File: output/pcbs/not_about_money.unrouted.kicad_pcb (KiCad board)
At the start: 2 copper layers, 76.5 x 114.5 mm, 53 parts

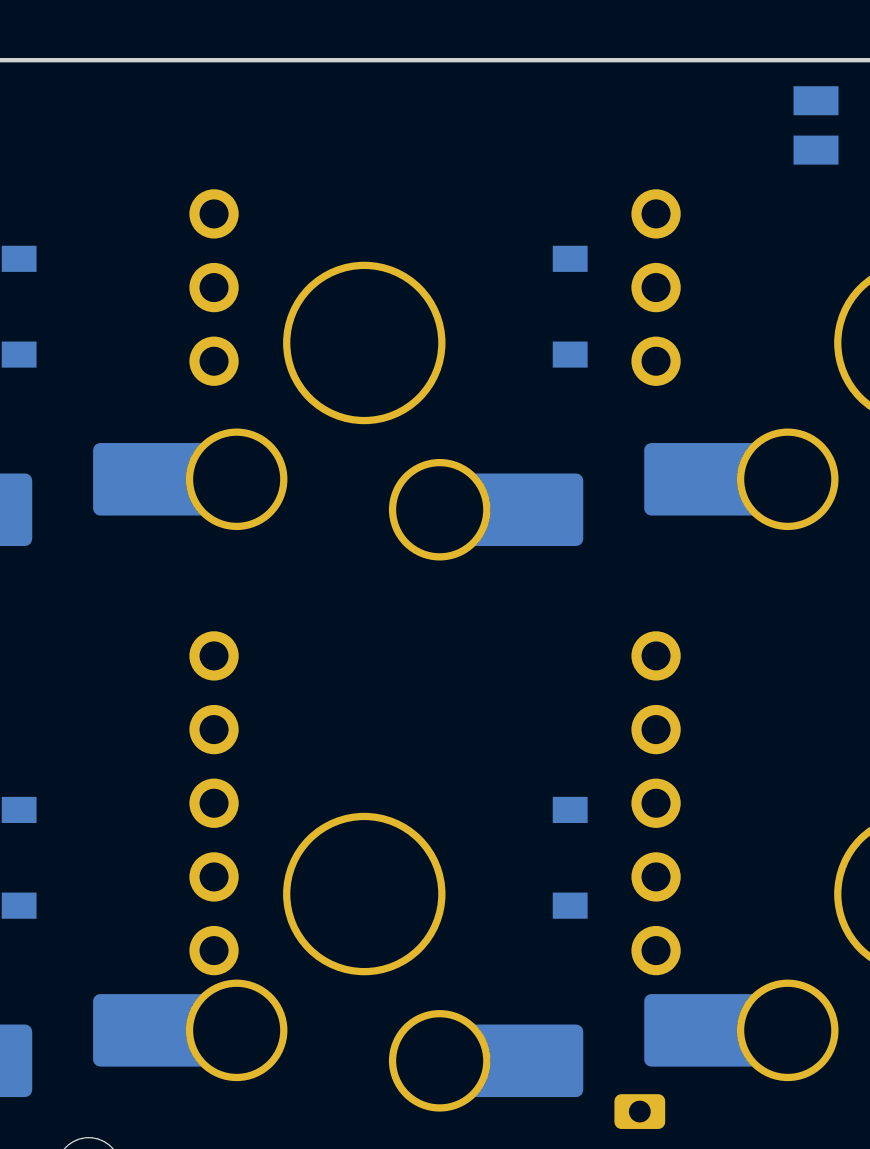
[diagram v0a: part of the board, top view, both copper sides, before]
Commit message: Move nice!nano 1.5mm to the edge, add its CAD model, USB scoop
- nice!nano v2 STEP (kicad/3d/) is now the authority for the case's nano
  and USB-C geometry, and the MCU footprint's 3D model (rotate -90,
  offset 0.11/2.45, verified by exporting the board to STEP).
- MCU moved 1.5mm toward the top edge (KiCad y 13.25 -> 11.75): nano edge
  flush with the PCB edge, USB-C 0.96 past it. Pin clearance improves to
  >=1.51. Re-routed (RAW re-routed alone after freerouting ran it over a
  PWR1 no-net pad); DRC 0 errors, 0 unconnected.
- Case: USB window from the CAD model with 0.25 clearance, a 12.5x6.5 r1.5
  cable-head scoop whose back wall is flush with the USB mouth (collar
  inside the cavity only when the mouth sits behind the wall).
- Fab: kicad/scripts/export_all.sh regenerates fab/, the PCBWay package
  and the board renders; both recipes reproduce the 2026-10-01 exports of
  the old board. All outputs regenerated for the new board.

Co-Authored-By: Claude Opus 5.5 <noreply@anthropic.com>
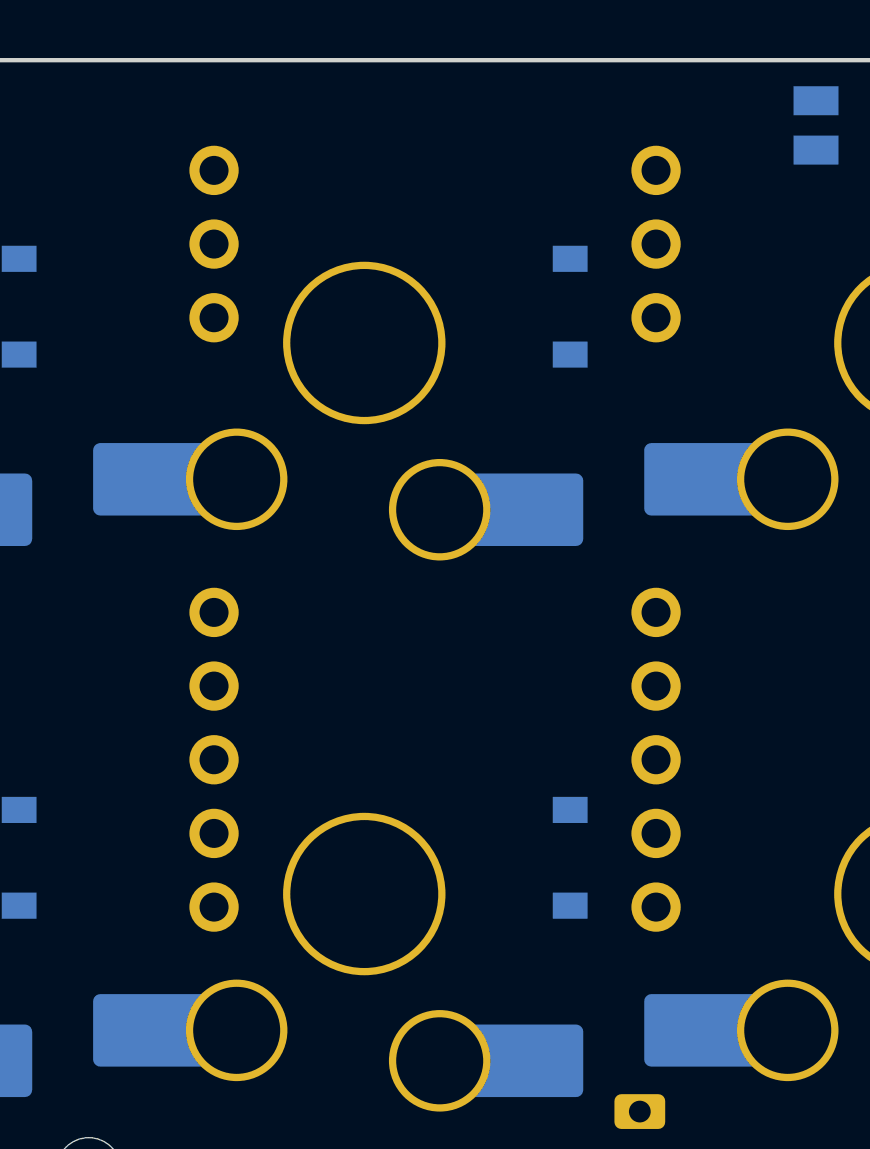
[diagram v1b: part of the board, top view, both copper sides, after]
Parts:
- moved MCU1 1.50 mm to (121.4, 11.8)
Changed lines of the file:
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@@
   (title_block
     (title "not_about_money")
-    (date "2026-10-02")
+    (date "2026-10-05")
     (rev "v1.0.0")
     (company "Unknown")
@@
   (footprint "ceoloide:mcu_nice_nano"
     (layer "B.Cu")
-    (at 121.44 13.25 0)
+    (at 121.44 11.75 0)
     (property "Reference" "MCU1"
       (at 0 -15 0)
@@
     (fp_line (start 6.29 -14.03) (end 6.29 16.57) (layer "B.SilkS") (stroke (width 0.12) (type solid)))
     (fp_line (start 8.95 -11.43) (end 6.29 -11.43) (layer "B.SilkS") (stroke (width 0.12) (type solid)))
+    (model "${KIPRJMOD}/3d/nice_nano_v2.step"
+      (offset (xyz 0 0.11 2.45))
+      (scale (xyz 1 1 1))
+      (rotate (xyz 0 0 -90))
+    )
   )
   (footprint "ceoloide:power_switch_smd_side"
